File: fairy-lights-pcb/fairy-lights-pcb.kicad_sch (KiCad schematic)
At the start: 19 parts, among them J1 Power_Jack, J2 Conn_LED_Strand_SPI, J3 Conn_LED_Strand_WS2812, J4 Conn_I2C, J5 Conn_02x04_Top_Bottom, SW1 SW_PWR, SW2 USER_A, SW3 USER_B, U1 WeMos_D1_mini

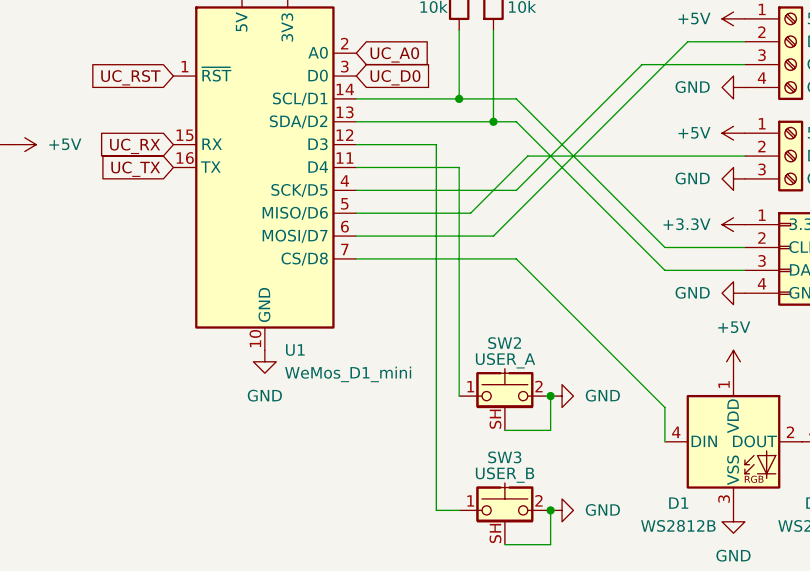
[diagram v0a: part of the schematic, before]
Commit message: Move USER_A button to pin D0
This allows using it to wake out of deep sleep, and avoids interactions
with the MCU module's built-in LED. The downside is that the pin has to
be polled in software while the MCU is running.
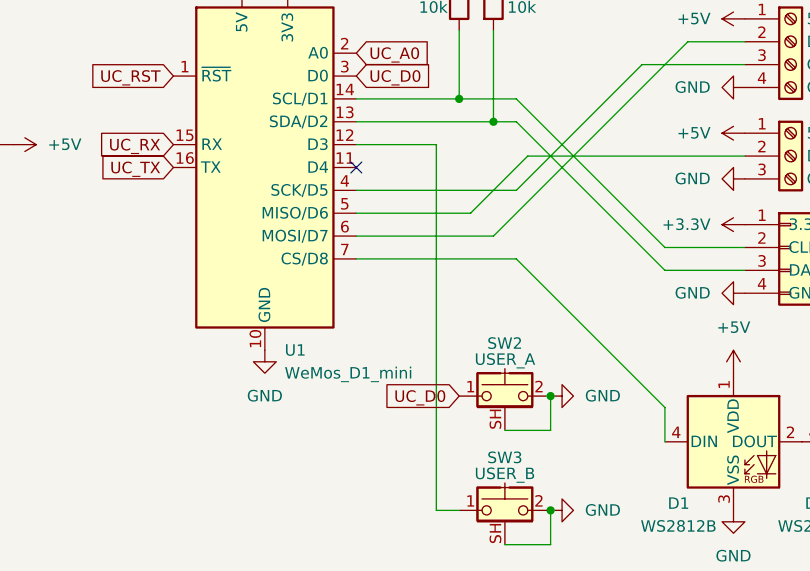
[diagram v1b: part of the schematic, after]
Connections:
- net UC_D0: now also SW2.1
- net at U1.11 (D4): no longer SW2.1
- no-connect marks 1 -> 2
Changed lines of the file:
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@@
+	)
+	(no_connect
+		(at 124.46 76.2)
 	)
 	(no_connect
@@
 	(wire
 		(pts
-			(xy 124.46 76.2) (xy 135.89 76.2)
-		)
-		(stroke
-			(width 0)
-			(type default)
-		)
-	)
-	(wire
-		(pts
 			(xy 124.46 83.82) (xy 139.7 83.82)
 		)
@@
 		(pts
 			(xy 124.46 81.28) (xy 137.16 81.28)
-		)
-		(stroke
-			(width 0)
-			(type default)
-		)
-	)
-	(wire
-		(pts
-			(xy 135.89 76.2) (xy 135.89 101.6)
 		)
 		(stroke
@@
 			(effects
 				(font
+					(size 1.27 1.27)
+				)
+				(justify right)
+				(hide yes)
+			)
+		)
+	)
+	(global_label "UC_D0"
+		(shape input)
+		(at 135.89 101.6 180)
+		(fields_autoplaced yes)
+		(effects
+			(font
+				(size 1.27 1.27)
+			)
+			(justify right)
+		)
+		(property "Intersheetrefs" "${INTERSHEET_REFS}"
+			(at 126.8572 101.6 0)
+			(effects
+				(font

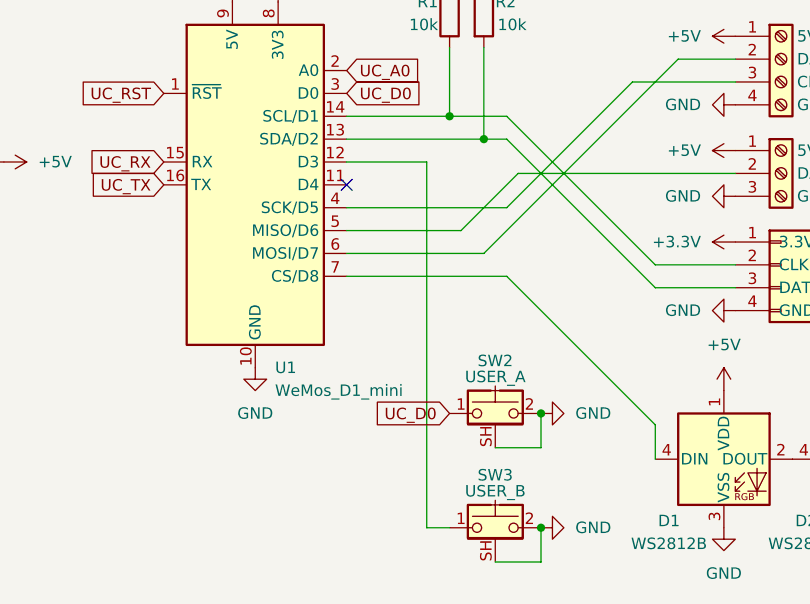
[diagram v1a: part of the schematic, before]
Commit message: Tweak button pin assignment
Button USER_A is now assigned to pin D3, button USER_B to pin D0.

Since this device is ultimately meant to be mains-powered, deep sleep
support is not a priority (additionally, while the MCU is sleeping,
the LED strand cannot quickly react to external requests delivered via
WiFi). Therefore, now, button USER_A can act as a soft power button (it
can even raise interrupts to wake from light sleep!) and also as a
flashing-mode button, while button USER_B can be used when the board
is fully online.
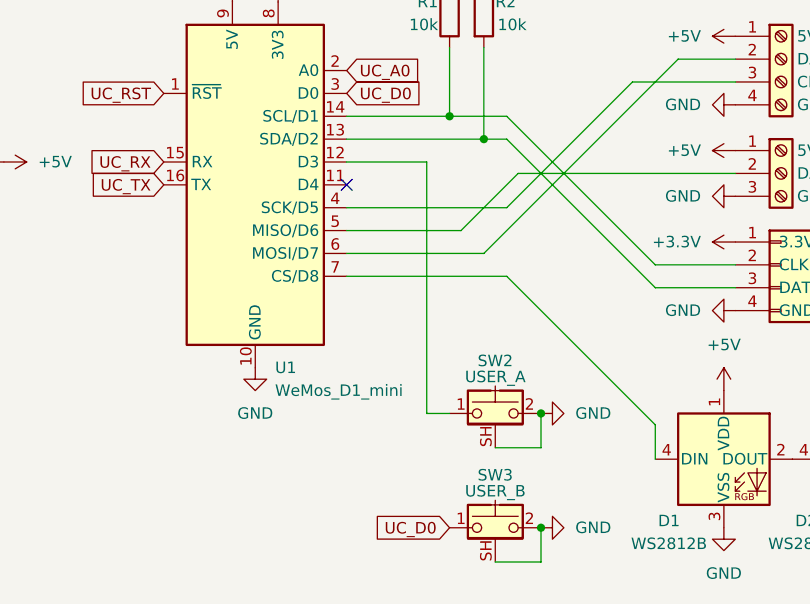
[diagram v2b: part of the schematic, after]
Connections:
- net UC_D0: now also SW3.1; no longer SW2.1
- net at U1.12 (D3): now also SW2.1; no longer SW3.1
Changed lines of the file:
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@@
 	(wire
 		(pts
-			(xy 133.35 73.66) (xy 133.35 114.3)
+			(xy 133.35 73.66) (xy 133.35 101.6)
 		)
 		(stroke
@@
 	(wire
 		(pts
-			(xy 133.35 114.3) (xy 135.89 114.3)
-		)
-		(stroke
-			(width 0)
-			(type default)
-		)
-	)
-	(wire
-		(pts
 			(xy 124.46 71.12) (xy 139.7 71.12)
 		)
@@
 		(pts
 			(xy 143.51 74.93) (xy 167.64 74.93)
+		)
+		(stroke
+			(width 0)
+			(type default)
+		)
+	)
+	(wire
+		(pts
+			(xy 133.35 101.6) (xy 135.89 101.6)
 		)
 		(stroke
@@
 	(global_label "UC_D0"
 		(shape input)
-		(at 135.89 101.6 180)
+		(at 135.89 114.3 180)
 		(fields_autoplaced yes)
 		(effects
@@
 		)
 		(property "Intersheetrefs" "${INTERSHEET_REFS}"
-			(at 126.8572 101.6 0)
-			(effects
-				(font
+			(at 126.8572 114.3 0)
+			(effects
+				(font

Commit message: Update PCB to use Turbocase-enabled footprints
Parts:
- J1: footprint Connector_BarrelJack:BarrelJack_Horizontal -> CustomLibrary:BarrelJack_Horizontal
- U1: footprint Module:WEMOS_D1_mini_light -> CustomLibrary:WEMOS_D1_mini_light
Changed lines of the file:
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@@
 			)
 		)
-		(property "Footprint" "Connector_BarrelJack:BarrelJack_Horizontal"
+		(property "Footprint" "CustomLibrary:BarrelJack_Horizontal"
 			(at 52.07 77.216 0)
 			(effects
@@
 			)
 		)
-		(property "Footprint" "Module:WEMOS_D1_mini_light"
+		(property "Footprint" "CustomLibrary:WEMOS_D1_mini_light"
 			(at 114.3 105.41 0)
 			(effects

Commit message: Update schematic and PCB to use correct D1 Mini
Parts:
- U1: symbol MCU_Module:WeMos_D1_mini -> RF_Module:WEMOS_D1_mini
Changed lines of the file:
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@@
 	)
 	(symbol
-		(lib_id "MCU_Module:WeMos_D1_mini")
+		(lib_id "RF_Module:WEMOS_D1_mini")
 		(at 114.3 76.2 0)
 		(unit 1)

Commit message: Add case cutouts for screw terminals
Sheesh, those crimped wire ends are *huge*.
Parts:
- J2: footprint TerminalBlock_Phoenix:TerminalBlock_Phoenix_MKDS-1,5-4_1x04_P5.00mm_Horizontal -> CustomLibrary:TerminalBlock_LED_Strand_1x04
- J3: footprint TerminalBlock_Phoenix:TerminalBlock_Phoenix_MKDS-1,5-3_1x03_P5.00mm_Horizontal -> CustomLibrary:TerminalBlock_LED_Strand_1x03
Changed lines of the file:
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@@
 			)
 		)
-		(property "Footprint" "TerminalBlock_Phoenix:TerminalBlock_Phoenix_MKDS-1,5-3_1x03_P5.00mm_Horizontal"
+		(property "Footprint" "CustomLibrary:TerminalBlock_LED_Strand_1x03"
 			(at 172.72 74.93 0)
 			(effects
@@
 			)
 		)
-		(property "Footprint" "TerminalBlock_Phoenix:TerminalBlock_Phoenix_MKDS-1,5-4_1x04_P5.00mm_Horizontal"
+		(property "Footprint" "CustomLibrary:TerminalBlock_LED_Strand_1x04"
 			(at 172.72 62.23 0)
 			(effects

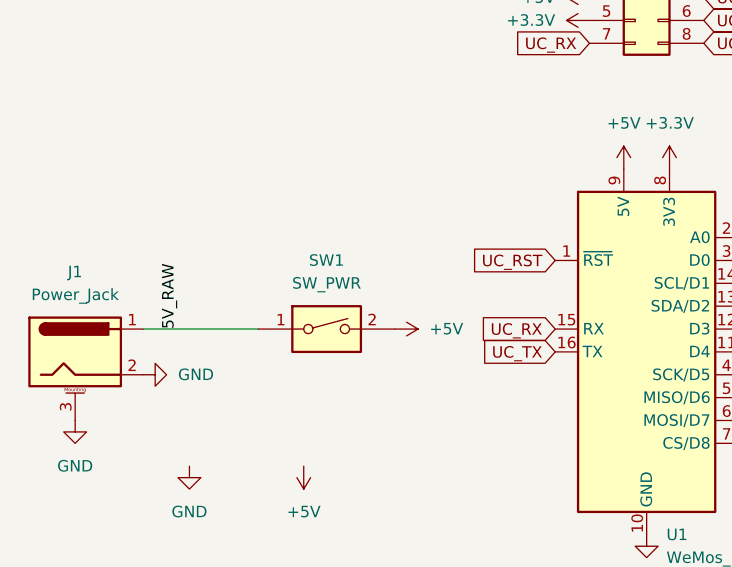
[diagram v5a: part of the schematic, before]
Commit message: Change power header to custom footprint
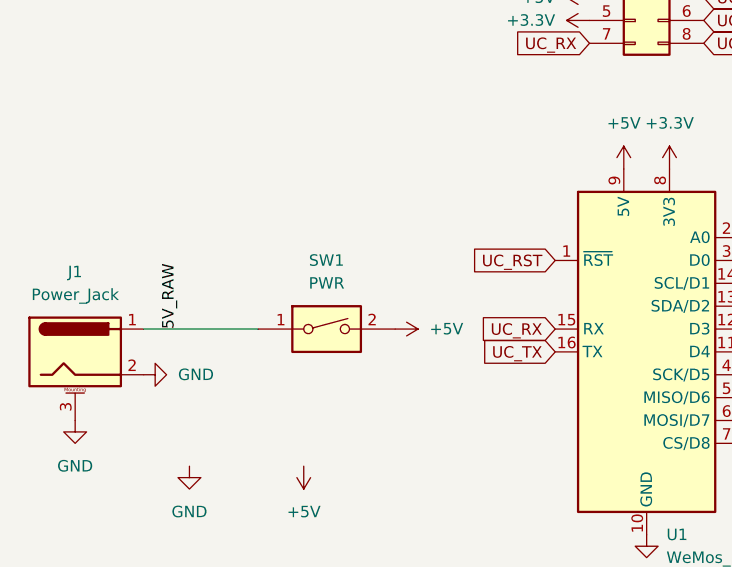
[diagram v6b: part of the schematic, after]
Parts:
- SW1: value SW_PWR -> PWR; footprint Connector_PinHeader_2.54mm:PinHeader_1x02_P2.54mm_Vertical -> CustomLibrary:PinHeader_Power
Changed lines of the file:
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@@
 	(label "5V_RAW"
 		(at 62.23 73.66 90)
-		(fields_autoplaced yes)
 		(effects
 			(font
@@
 			)
 		)
-		(property "Value" "SW_PWR"
+		(property "Value" "PWR"
 			(at 78.74 68.58 0)
 			(effects
@@
 			)
 		)
-		(property "Footprint" "Connector_PinHeader_2.54mm:PinHeader_1x02_P2.54mm_Vertical"
+		(property "Footprint" "CustomLibrary:PinHeader_Power"
 			(at 78.74 73.66 0)
 			(effects
